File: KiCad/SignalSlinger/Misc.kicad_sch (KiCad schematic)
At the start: 13 parts

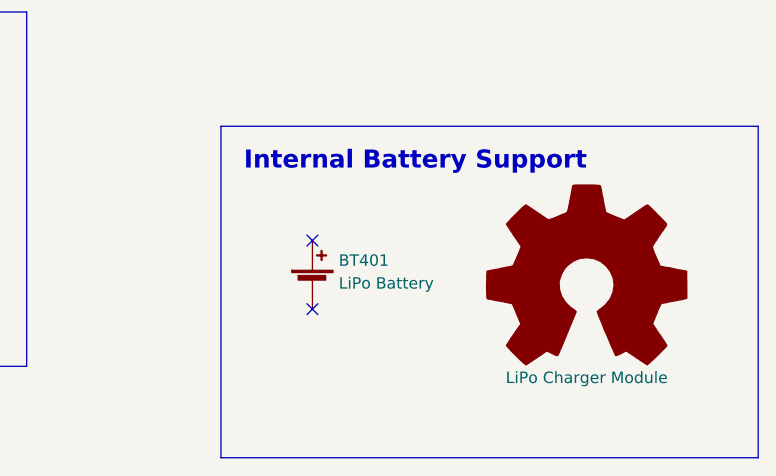
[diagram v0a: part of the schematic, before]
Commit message: Four Layers
Changed to a four-layer board, mostly for thermal flow reasons, but it also significantly improves ground plane coverage and voltage routing.
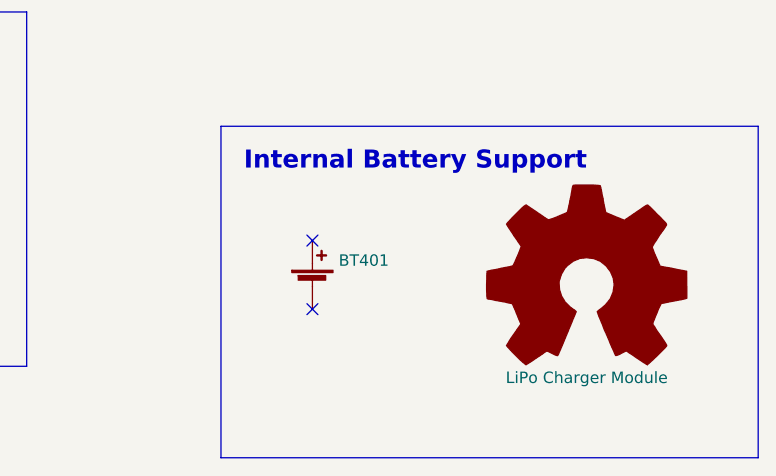
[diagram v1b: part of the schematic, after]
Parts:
- BT401: value LiPo Battery -> (none); Link https://www.adafruit.com/product/258 -> https://www.adafruit.com/product/1570; Manufacturer PN 258 -> 1570
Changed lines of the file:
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@@
       (effects (font (size 1.27 1.27)) (justify left))
     )
-    (property "Value" "LiPo Battery" (id 1) (at 208.661 144.4502 0)
+    (property "Value" "" (id 1) (at 208.661 144.4502 0)
       (effects (font (size 1.27 1.27)) (justify left))
     )
@@
       (effects (font (size 1.27 1.27)) hide)
     )
-    (property "Link" "https://www.adafruit.com/product/258" (id 4) (at 205.74 144.78 0)
+    (property "Link" "https://www.adafruit.com/product/1570" (id 4) (at 205.74 144.78 0)
       (effects (font (size 1.27 1.27)) hide)
     )
@@
       (effects (font (size 1.27 1.27)) hide)
     )
-    (property "Manufacturer PN" "258" (id 6) (at 205.74 144.78 0)
+    (property "Manufacturer PN" "1570" (id 6) (at 205.74 144.78 0)
       (effects (font (size 1.27 1.27)) hide)
     )
-    (property "Description" "Lithium Ion Polymer Battery - 3.7v 1200mAh" (id 7) (at 205.74 144.78 0)
+    (property "Description" "Lithium Ion Polymer Battery - 3.7v 100mAh" (id 7) (at 205.74 144.78 0)
       (effects (font (size 1.27 1.27)) hide)
     )

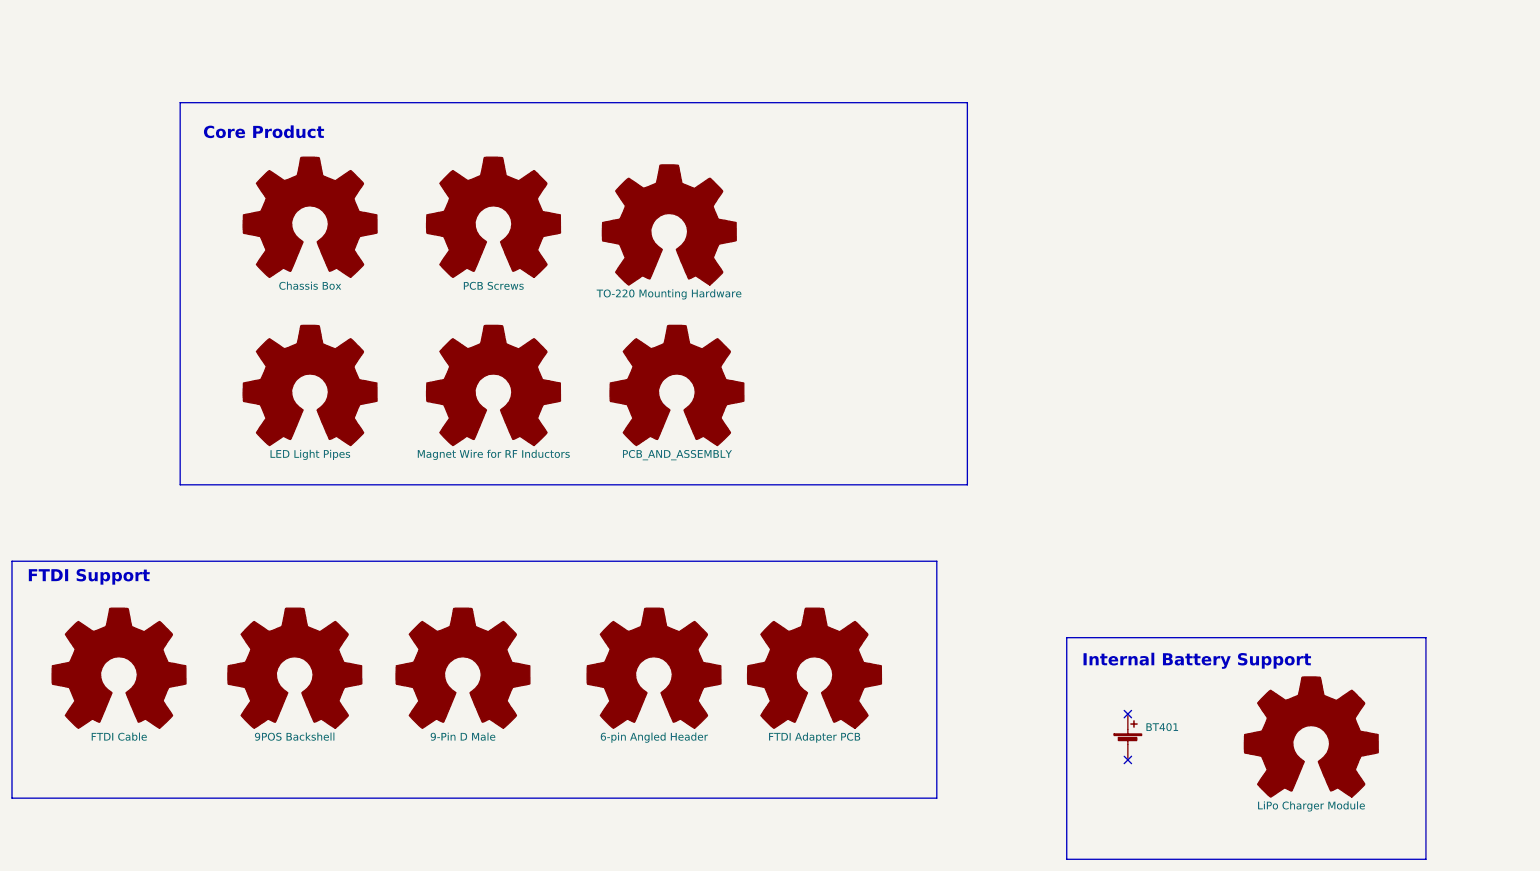
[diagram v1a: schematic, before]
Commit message: Schematic and PCB Update
Added jumpers for Foxoring operation
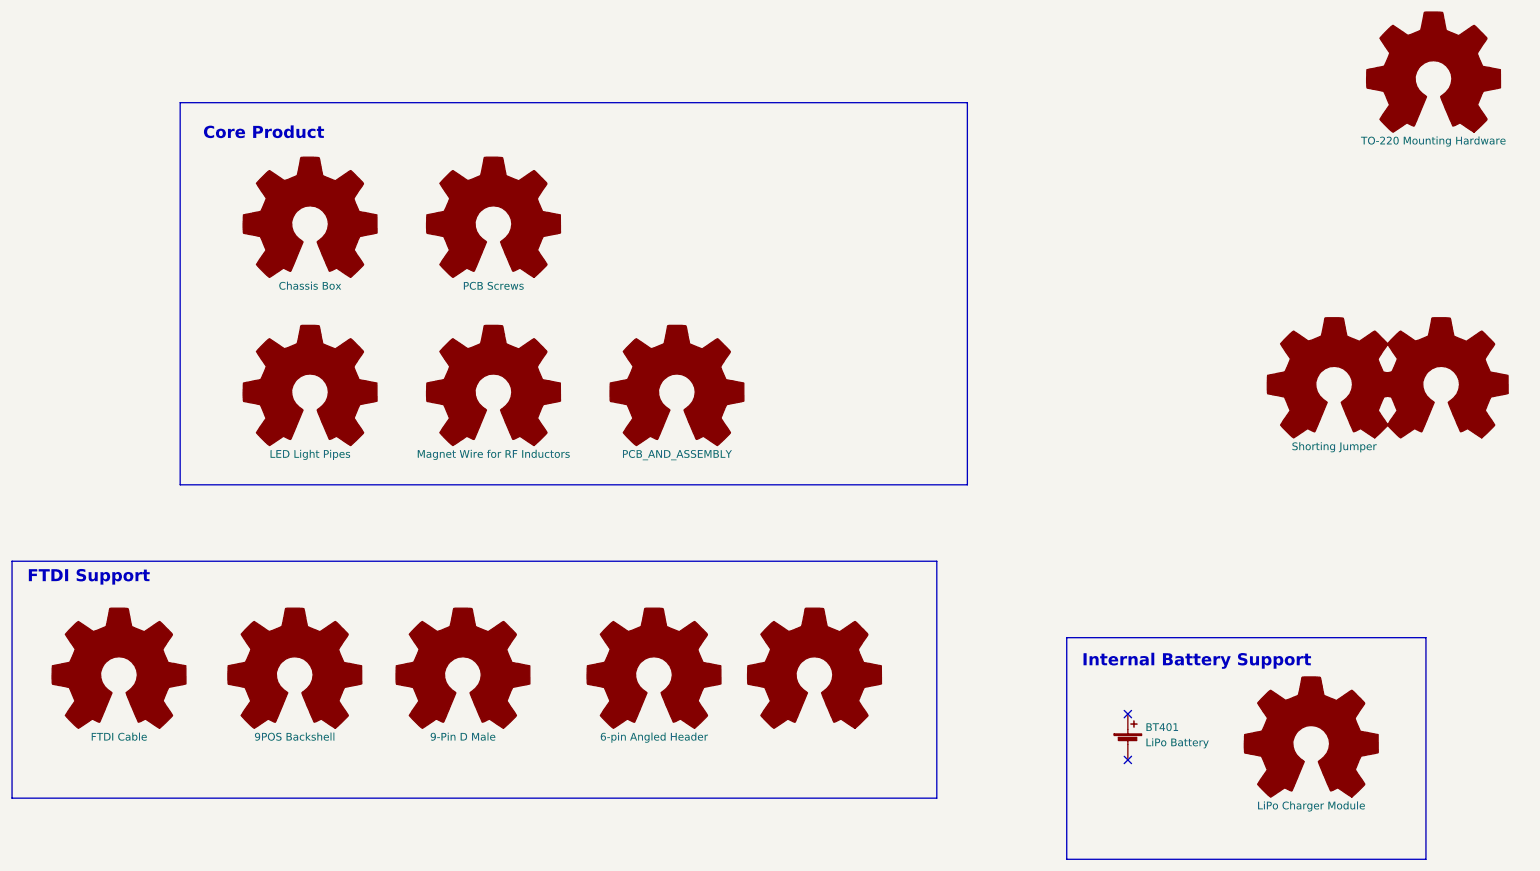
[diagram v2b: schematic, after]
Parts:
- added HDWR412: (no value), symbol Graphic:Logo_Open_Hardware_Large
- added HDWR414: Shorting Jumper, symbol Graphic:Logo_Open_Hardware_Large
- BT401: value (none) -> LiPo Battery
- HDWR413: value FTDI Adapter PCB -> (none); Link (none) -> https://oshpark.com/shared_projects/15SnDRmB
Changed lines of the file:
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@@
     )
   )
-  (symbol (lib_id "Graphic:Logo_Open_Hardware_Large") (at 129.54 59.69 0) (unit 1)
+  (symbol (lib_id "Graphic:Logo_Open_Hardware_Large") (at 240.03 85.09 0) (unit 1)
     (in_bom yes) (on_board yes) (fields_autoplaced)
-    (property "Reference" "HDWR411" (id 0) (at 129.54 46.99 0)
+    (property "Reference" "HDWR414" (id 0) (at 240.03 72.39 0)
       (effects (font (size 1.27 1.27)) hide)
     )
-    (property "Value" "TO-220 Mounting Hardware" (id 1) (at 129.54 69.85 0))
-    (property "Footprint" "" (id 2) (at 129.54 59.69 0)
+    (property "Value" "Shorting Jumper" (id 1) (at 240.03 95.25 0))
+    (property "Footprint" "" (id 2) (at 240.03 85.09 0)
       (effects (font (size 1.27 1.27)) hide)
     )
-    (property "Datasheet" "" (id 3) (at 129.54 59.69 0)
+    (property "Datasheet" "" (id 3) (at 240.03 85.09 0)
       (effects (font (size 1.27 1.27)) hide)
     )
-    (property "Digi-Key Part No." "Amazon" (id 4) (at 129.54 59.69 0)
+    (property "Digi-Key Part No." "S9345-ND" (id 4) (at 240.03 85.09 0)
+      (effects (font (size 1.27 1.27)) hide)
+    )
+    (property "Link" "https://www.digikey.com/short/w0p92mhw" (id 5) (at 240.03 85.09 0)
+      (effects (font (size 1.27 1.27)) hide)
+    )
+    (property "Manufacturer" "Sullins Connector Solutions" (id 6) (at 240.03 85.09 0)
+      (effects (font (size 1.27 1.27)) hide)
+    )
+    (property "Manufacturer PN" "NPB02SVAN-RC" (id 7) (at 240.03 85.09 0)
+      (effects (font (size 1.27 1.27)) hide)
+    )
+    (property "Description" "CONN JUMPER SHORTING 1.27MM GOLD" (id 8) (at 240.03 85.09 0)
+      (effects (font (size 1.27 1.27)) hide)
+    )
+  )
+  (symbol (lib_id "Graphic:Logo_Open_Hardware_Large") (at 256.54 34.29 0) (unit 1)
+    (in_bom yes) (on_board yes) (fields_autoplaced)
+    (property "Reference" "HDWR411" (id 0) (at 256.54 21.59 0)
+      (effects (font (size 1.27 1.27)) hide)
+    )
+    (property "Value" "TO-220 Mounting Hardware" (id 1) (at 256.54 44.45 0))
+    (property "Footprint" "" (id 2) (at 256.54 34.29 0)
+      (effects (font (size 1.27 1.27)) hide)
+    )
+    (property "Datasheet" "" (id 3) (at 256.54 34.29 0)
+      (effects (font (size 1.27 1.27)) hide)
+    )
+    (property "Digi-Key Part No." "Amazon" (id 4) (at 256.54 34.29 0)
       (effects (font (size 1.27 1.27)) hide)
     )
@@
       (effects (font (size 1.27 1.27)) hide)
     )
-    (property "Value" "FTDI Adapter PCB" (id 1) (at 153.67 143.51 0))
+    (property "Value" "" (id 1) (at 153.67 143.51 0))
     (property "Footprint" "" (id 2) (at 153.67 133.35 0)
       (effects (font (size 1.27 1.27)) hide)
     )
     (property "Datasheet" "" (id 3) (at 153.67 133.35 0)
+      (effects (font (size 1.27 1.27)) hide)
+    )
+    (property "Link" "https://oshpark.com/shared_projects/15SnDRmB" (id 4) (at 153.67 133.35 0)
+      (effects (font (size 1.27 1.27)) hide)
+    )
+  )
+  (symbol (lib_id "Graphic:Logo_Open_Hardware_Large") (at 257.81 85.09 0) (unit 1)
+    (in_bom yes) (on_board yes) (fields_autoplaced)
+    (property "Reference" "HDWR412" (id 0) (at 257.81 72.39 0)
+      (effects (font (size 1.27 1.27)) hide)
+    )
+    (property "Value" "" (id 1) (at 257.81 95.25 0))
+    (property "Footprint" "" (id 2) (at 257.81 85.09 0)
+      (effects (font (size 1.27 1.27)) hide)
+    )
+    (property "Datasheet" "" (id 3) (at 257.81 85.09 0)
+      (effects (font (size 1.27 1.27)) hide)
+    )
+    (property "Digi-Key Part No." "S9345-ND" (id 4) (at 257.81 85.09 0)
+      (effects (font (size 1.27 1.27)) hide)
+    )
+    (property "Link" "https://www.digikey.com/short/w0p92mhw" (id 5) (at 257.81 85.09 0)
+      (effects (font (size 1.27 1.27)) hide)
+    )
+    (property "Manufacturer" "Sullins Connector Solutions" (id 6) (at 257.81 85.09 0)
+      (effects (font (size 1.27 1.27)) hide)
+    )
+    (property "Manufacturer PN" "NPB02SVAN-RC" (id 7) (at 257.81 85.09 0)
+      (effects (font (size 1.27 1.27)) hide)
+    )
+    (property "Description" "CONN JUMPER SHORTING 1.27MM GOLD" (id 8) (at 257.81 85.09 0)
       (effects (font (size 1.27 1.27)) hide)
     )
@@
       (effects (font (size 1.27 1.27)) (justify left))
     )
-    (property "Value" "" (id 1) (at 208.661 144.4502 0)
+    (property "Value" "LiPo Battery" (id 1) (at 208.661 144.4502 0)
       (effects (font (size 1.27 1.27)) (justify left))
     )

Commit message: Rev 3.2
Schematic and PCB update
Regenerated Gerbers, schematic.pdf, BOM docs
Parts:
- HDWR412: value (none) -> Shorting Jumper
- HDWR413: value (none) -> FTDI Adapter PCB
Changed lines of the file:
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@@
   (title_block
     (title "SignalSlinger")
-    (date "2024-04-30")
-    (rev "3.1")
+    (date "2024-05-06")
+    (rev "3.2")
   )
   (no_connect (at 205.74 147.32))
@@
       (effects (font (size 1.27 1.27)) hide)
     )
-    (property "Value" "" (id 1) (at 153.67 143.51 0))
+    (property "Value" "FTDI Adapter PCB" (id 1) (at 153.67 143.51 0))
     (property "Footprint" "" (id 2) (at 153.67 133.35 0)
       (effects (font (size 1.27 1.27)) hide)
@@
       (effects (font (size 1.27 1.27)) hide)
     )
-    (property "Value" "" (id 1) (at 257.81 95.25 0))
+    (property "Value" "Shorting Jumper" (id 1) (at 257.81 95.25 0))
     (property "Footprint" "" (id 2) (at 257.81 85.09 0)
       (effects (font (size 1.27 1.27)) hide)
